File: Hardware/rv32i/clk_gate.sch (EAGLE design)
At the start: 11 parts, among them IC1 SN74ACT08D, IC2 SN74ACT08D, IC3 SN74ACT08D, IC4 SN74ACT08D, IC5 SN74ACT08D, IC6 SN74ACT08D, IC7 SN74ACT08D, IC8 SN74ACT08D

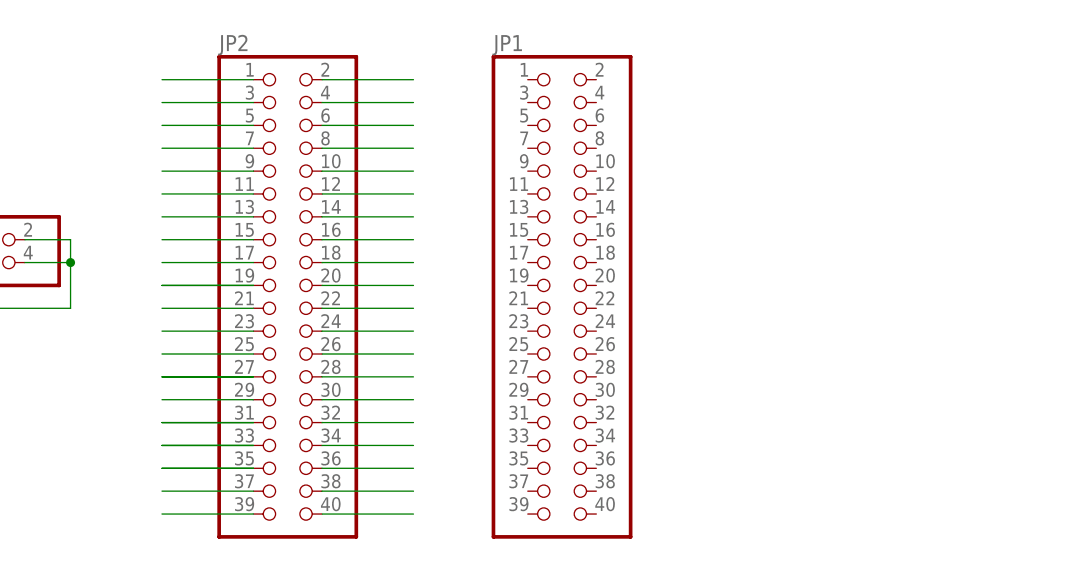
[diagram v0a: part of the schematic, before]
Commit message: Clock Gate
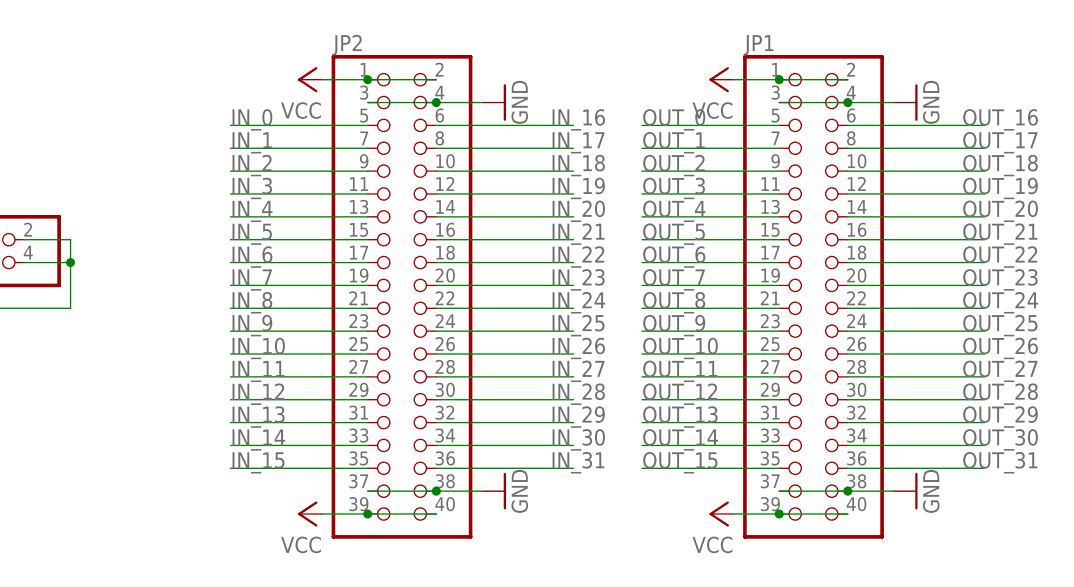
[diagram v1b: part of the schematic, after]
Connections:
- removed net N$1: JP2.1
- removed net N$10: JP2.19
- removed net N$12: JP2.21
- removed net N$13: JP2.23
- removed net N$14: JP2.25
- removed net N$15: JP2.27
- removed net N$17: JP2.29
- removed net N$18: JP2.31
- removed net N$19: JP2.33
- removed net N$2: JP2.3
- removed net N$20: JP2.35
- removed net N$24: JP2.37
- removed net N$25: JP2.39
- removed net N$26: JP2.32
- removed net N$27: JP2.34
- removed net N$28: JP2.36
- removed net N$29: JP2.38
- removed net N$3: JP2.5
- removed net N$30: JP2.40
- removed net N$31: JP2.22
- removed net N$32: JP2.24
- removed net N$33: JP2.26
- removed net N$34: JP2.28
- removed net N$35: JP2.30
- removed net N$36: JP2.12
- removed net N$37: JP2.14
- removed net N$38: JP2.16
- removed net N$39: JP2.18
- removed net N$4: JP2.7
- removed net N$40: JP2.20
- removed net N$41: JP2.2
- removed net N$42: JP2.4
- removed net N$43: JP2.6
- removed net N$44: JP2.8
- removed net N$45: JP2.10
- removed net N$5: JP2.9
- removed net N$6: JP2.11
- removed net N$7: JP2.13
- removed net N$8: JP2.15
- removed net N$9: JP2.17
- net GND: now also JP1.3, JP1.37, JP1.38, JP1.4, JP2.3, JP2.37, JP2.38, JP2.4
- net IN_0: now also JP2.5
- net IN_1: now also JP2.7
- net IN_10: now also JP2.25
- net IN_11: now also JP2.27
- net IN_12: now also JP2.29
- net IN_13: now also JP2.31
- net IN_14: now also JP2.33
- net IN_15: now also JP2.35
- net IN_16: now also JP2.6
- net IN_17: now also JP2.8
- net IN_18: now also JP2.10
- net IN_19: now also JP2.12
- net IN_2: now also JP2.9
- net IN_20: now also JP2.14
- net IN_21: now also JP2.16
- net IN_22: now also JP2.18
- net IN_23: now also JP2.20
- net IN_24: now also JP2.22
- net IN_25: now also JP2.24
- net IN_26: now also JP2.26
- net IN_27: now also JP2.28
- net IN_28: now also JP2.30
- net IN_29: now also JP2.32
- net IN_3: now also JP2.11
- net IN_30: now also JP2.34
- net IN_31: now also JP2.36
- net IN_4: now also JP2.13
- net IN_5: now also JP2.15
- net IN_6: now also JP2.17
- net IN_7: now also JP2.19
- net IN_8: now also JP2.21
- net IN_9: now also JP2.23
- net OUT_0: now also JP1.5
- net OUT_1: now also JP1.7
- net OUT_10: now also JP1.25
- net OUT_11: now also JP1.27
- net OUT_12: now also JP1.29
- net OUT_13: now also JP1.31
- net OUT_14: now also JP1.33
- net OUT_15: now also JP1.35
- net OUT_16: now also JP1.6
- net OUT_17: now also JP1.8
- net OUT_18: now also JP1.10
- net OUT_19: now also JP1.12
- net OUT_2: now also JP1.9
- net OUT_20: now also JP1.14
- net OUT_21: now also JP1.16
- net OUT_22: now also JP1.18
- net OUT_23: now also JP1.20
- net OUT_24: now also JP1.22
- net OUT_25: now also JP1.24
- net OUT_26: now also JP1.26
- net OUT_27: now also JP1.28
- net OUT_28: now also JP1.30
- net OUT_29: now also JP1.32
- net OUT_3: now also JP1.11
- net OUT_30: now also JP1.34
- net OUT_31: now also JP1.36
- net OUT_4: now also JP1.13
- net OUT_5: now also JP1.15
- net OUT_6: now also JP1.17
- net OUT_7: now also JP1.19
- net OUT_8: now also JP1.21
- net OUT_9: now also JP1.23
- net VCC: now also JP1.1, JP1.2, JP1.39, JP1.40, JP2.1, JP2.2, JP2.39, JP2.40
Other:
- moved on the sheet: JP1, JP2
